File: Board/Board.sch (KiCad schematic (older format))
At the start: 54 parts, among them J1 Screw_Terminal_1x02, P1 USB_B, P2 CONN_01X05, SW1 SW_SPST, SW2 SW_SPST, U1 MCP23016, U2 LM1117-3.3, U3 MCP9808, U4 ESP-12E

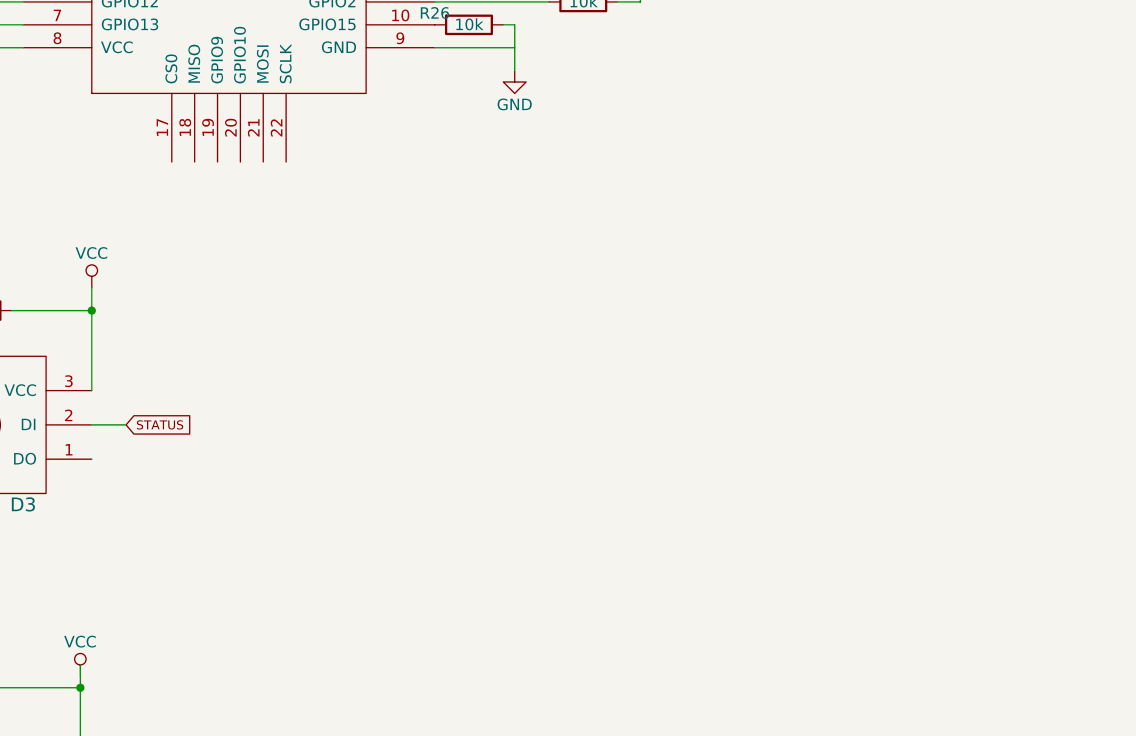
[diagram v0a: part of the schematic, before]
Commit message: Add an SPI connector
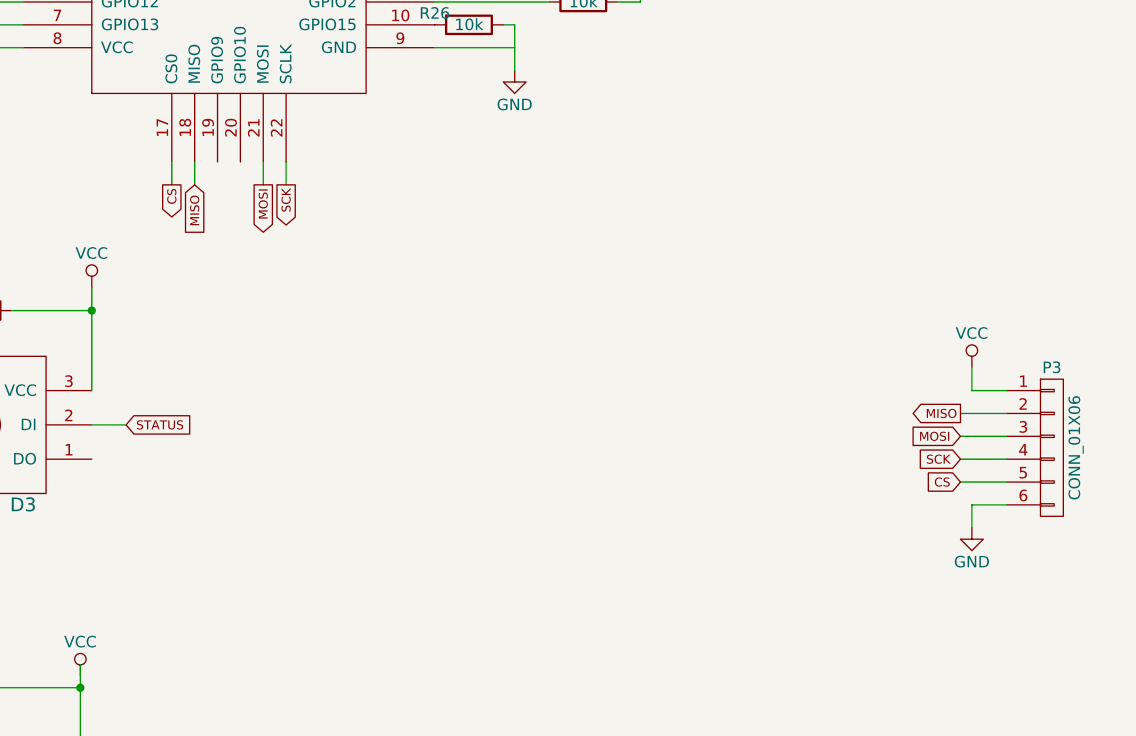
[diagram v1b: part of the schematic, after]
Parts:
- added P3: CONN_01X06, symbol CONN_01X06
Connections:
- net GND: now also P3.6 (P6)
- net VCC: now also P3.1 (P1)
- net CS: now reaches U4.17 (CS0)
- net CS: now also P3.5 (P5)
- net MISO: now reaches U4.18 (MISO)
- net MISO: now also P3.2 (P2)
- net MOSI: now reaches U4.21 (MOSI)
- net MOSI: now also P3.3 (P3)
- net SCK: now reaches U4.22 (SCLK)
- net SCK: now also P3.4 (P4)
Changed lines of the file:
@@
 $EndComp
 $Comp
-L VCC #PWR31
+L VCC #PWR33
 U 1 1 5AD1E910
 P 10400 1300
-F 0 "#PWR31" H 10400 1150 50  0001 C CNN
+F 0 "#PWR33" H 10400 1150 50  0001 C CNN
 F 1 "VCC" H 10400 1450 50  0000 C CNN
 F 2 "" H 10400 1300 50  0000 C CNN
@@
 $EndComp
 $Comp
-L VDD #PWR32
+L VDD #PWR34
 U 1 1 5AD1E925
 P 10600 1300
-F 0 "#PWR32" H 10600 1150 50  0001 C CNN
+F 0 "#PWR34" H 10600 1150 50  0001 C CNN
 F 1 "VDD" H 10600 1450 50  0000 C CNN
 F 2 "" H 10600 1300 50  0000 C CNN
@@
 Wire Wire Line
 	5100 2600 5000 2600
+$Comp
+L GND #PWR32
+U 1 1 5AD82799
+P 10050 5400
+F 0 "#PWR32" H 10050 5150 50  0001 C CNN
+F 1 "GND" H 10050 5250 50  0000 C CNN
+F 2 "" H 10050 5400 50  0000 C CNN
+F 3 "" H 10050 5400 50  0000 C CNN
+	1    10050 5400
+	1    0    0    -1
+$EndComp
+$Comp
+L VCC #PWR31
+U 1 1 5AD8279F
+P 10050 4700
+F 0 "#PWR31" H 10050 4550 50  0001 C CNN
+F 1 "VCC" H 10050 4850 50  0000 C CNN
+F 2 "" H 10050 4700 50  0000 C CNN
+F 3 "" H 10050 4700 50  0000 C CNN
+	1    10050 4700
+	1    0    0    -1
+$EndComp
+Wire Wire Line
+	10050 4700 10050 4800
+Wire Wire Line
+	10050 4800 10200 4800
+Wire Wire Line
+	10050 5400 10050 5300
+Wire Wire Line
+	10050 5300 10200 5300
+Text GLabel 10000 4900 0    39   Output ~ 0
+MISO
+Text GLabel 10000 5000 0    39   Input ~ 0
+MOSI
+Text GLabel 10000 5100 0    39   Input ~ 0
+SCK
+Wire Wire Line
+	10200 4900 10000 4900
+Wire Wire Line
+	10200 5000 10000 5000
+Wire Wire Line
+	10200 5100 10000 5100
+Text GLabel 6650 3900 3    39   Input ~ 0
+MISO
+Wire Wire Line
+	6650 3900 6650 3800
+Text GLabel 6950 3900 3    39   Output ~ 0
+MOSI
+Wire Wire Line
+	6950 3800 6950 3900
+Text GLabel 7050 3900 3    39   Output ~ 0
+SCK
+Wire Wire Line
+	7050 3900 7050 3800
+$Comp
+L CONN_01X06 P3
+U 1 1 5AD852A1
+P 10400 5050
+F 0 "P3" H 10400 5400 50  0000 C CNN
+F 1 "CONN_01X06" V 10500 5050 50  0000 C CNN
+F 2 "" H 10400 5050 50  0000 C CNN
+F 3 "" H 10400 5050 50  0000 C CNN
+	1    10400 5050
+	1    0    0    -1
+$EndComp
+Text GLabel 10000 5200 0    39   Input ~ 0
+CS
+Wire Wire Line
+	10000 5200 10200 5200
+Text GLabel 6550 3900 3    39   Output ~ 0
+CS
+Wire Wire Line
+	6550 3800 6550 3900
 $EndSCHEMATC

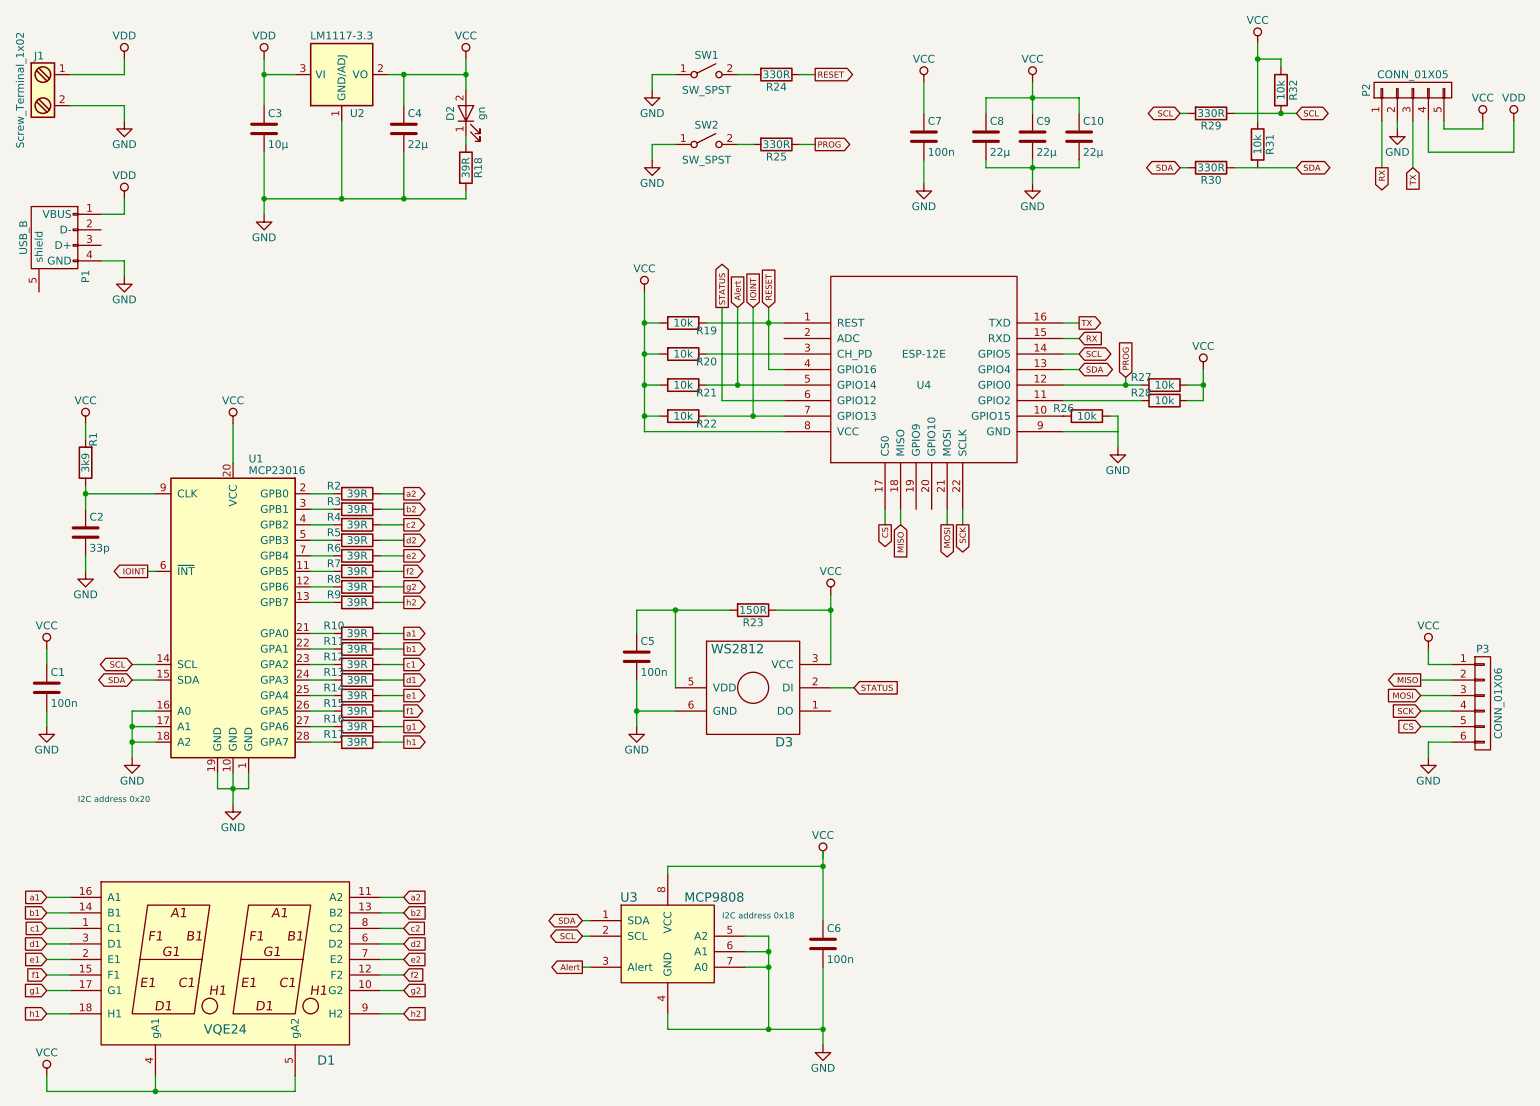
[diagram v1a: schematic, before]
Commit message: Move some things around in the schematic
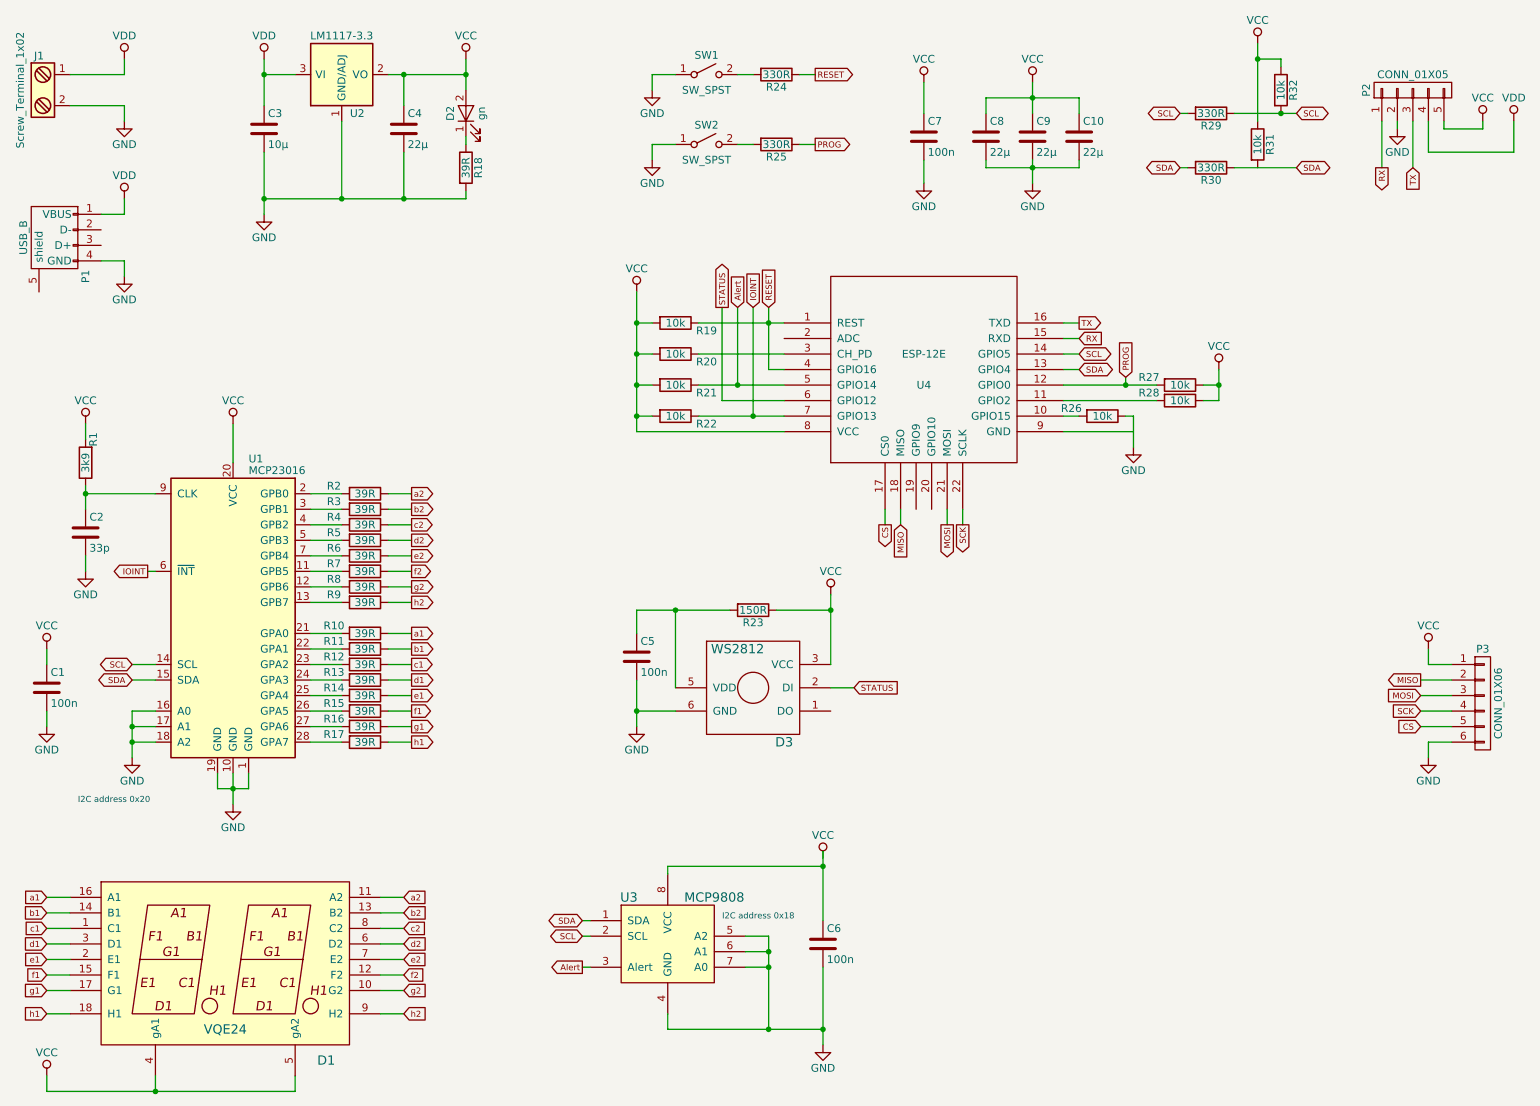
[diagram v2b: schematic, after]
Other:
- moved on the sheet: R10, R11, R12, R13, R14, R15, R16, R17, R19, R2, R20, R21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

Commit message: Remaining footprints
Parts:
- P2: footprint (none) -> Socket_Strips:Socket_Strip_Straight_1x05
- P3: footprint (none) -> Socket_Strips:Socket_Strip_Straight_1x06
- SW1, SW2: footprint (none) -> Buttons_Switches_SMD:SW_SPST_EVQPE1
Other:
- moved on the sheet: R25
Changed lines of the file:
@@
 Sheet 1 1
 Title "Cloud Temperature Sensor"
-Date "2018-04-17"
+Date "2018-04-21"
 Rev ""
 Comp "penguineer"
@@
 $EndComp
 $Comp
-L VCC #PWR17
+L VCC #PWR16
 U 1 1 5AD1E3D6
 P 4950 2400
-F 0 "#PWR17" H 4950 2250 50  0001 C CNN
+F 0 "#PWR16" H 4950 2250 50  0001 C CNN
 F 1 "VCC" H 4950 2550 50  0000 C CNN
 F 2 "" H 4950 2400 50  0000 C CNN
@@
 F 0 "P2" H 9950 1400 50  0000 C CNN
 F 1 "CONN_01X05" V 10050 1100 50  0000 C CNN
-F 2 "" H 9950 1100 50  0000 C CNN
+F 2 "Socket_Strips:Socket_Strip_Straight_1x05" H 9950 1100 50  0001 C CNN
 F 3 "" H 9950 1100 50  0000 C CNN
 	1    9950 1100
@@
 	4950 5100 5200 5100
 $Comp
-L GND #PWR16
+L GND #PWR17
 U 1 1 5AD4FEAF
 P 4950 5200
-F 0 "#PWR16" H 4950 4950 50  0001 C CNN
+F 0 "#PWR17" H 4950 4950 50  0001 C CNN
 F 1 "GND" H 4950 5050 50  0000 C CNN
 F 2 "" H 4950 5200 50  0000 C CNN
@@
 Wire Wire Line
 	3850 1800 3850 1750
-$Comp
-L SW_SPST SW1
-U 1 1 5AD68F78
-P 5400 1000
-F 0 "SW1" H 5400 1125 50  0000 C CNN
-F 1 "SW_SPST" H 5400 900 50  0000 C CNN
-F 2 "" H 5400 1000 50  0000 C CNN
-F 3 "" H 5400 1000 50  0000 C CNN
-	1    5400 1000
-	1    0    0    -1
-$EndComp
 Text GLabel 6100 1000 2    39   Output ~ 0
 RESET
@@
 Wire Wire Line
 	5050 1000 5200 1000
-$Comp
-L SW_SPST SW2
-U 1 1 5AD69C50
-P 5400 1450
-F 0 "SW2" H 5400 1575 50  0000 C CNN
-F 1 "SW_SPST" H 5400 1350 50  0000 C CNN
-F 2 "" H 5400 1450 50  0000 C CNN
-F 3 "" H 5400 1450 50  0000 C CNN
-	1    5400 1450
-	1    0    0    -1
-$EndComp
-Text GLabel 6100 1450 2    39   Output ~ 0
+Text GLabel 6100 1400 2    39   Output ~ 0
 PROG
 Wire Wire Line
-	5600 1450 5700 1450
+	5600 1400 5700 1400
 $Comp
 L GND #PWR19
 U 1 1 5AD69C58
-P 5050 1550
-F 0 "#PWR19" H 5050 1300 50  0001 C CNN
-F 1 "GND" H 5050 1400 50  0000 C CNN
-F 2 "" H 5050 1550 50  0000 C CNN
-F 3 "" H 5050 1550 50  0000 C CNN
-	1    5050 1550
-	1    0    0    -1
-$EndComp
-Wire Wire Line
-	5050 1550 5050 1450
-Wire Wire Line
-	5050 1450 5200 1450
+P 5050 1500
+F 0 "#PWR19" H 5050 1250 50  0001 C CNN
+F 1 "GND" H 5050 1350 50  0000 C CNN
+F 2 "" H 5050 1500 50  0000 C CNN
+F 3 "" H 5050 1500 50  0000 C CNN
+	1    5050 1500
+	1    0    0    -1
+$EndComp
+Wire Wire Line
+	5050 1500 5050 1400
+Wire Wire Line
+	5050 1400 5200 1400
 $Comp
 L R R24
@@
 L R R25
 U 1 1 5AD6C15E
-P 5850 1450
-F 0 "R25" V 5930 1450 50  0000 C CNN
-F 1 "330R" V 5850 1450 50  0000 C CNN
-F 2 "Resistors_SMD:R_0603_HandSoldering" V 5780 1450 50  0001 C CNN
-F 3 "" H 5850 1450 50  0000 C CNN
-	1    5850 1450
+P 5850 1400
+F 0 "R25" V 5930 1400 50  0000 C CNN
+F 1 "330R" V 5850 1400 50  0000 C CNN
+F 2 "Resistors_SMD:R_0603_HandSoldering" V 5780 1400 50  0001 C CNN
+F 3 "" H 5850 1400 50  0000 C CNN
+	1    5850 1400
 	0    1    1    0
 $EndComp
@@
 	6000 1000 6100 1000
 Wire Wire Line
-	6000 1450 6100 1450
+	6000 1400 6100 1400
 Wire Wire Line
 	5700 2500 5700 3200
@@
 F 0 "P3" H 10400 5400 50  0000 C CNN
 F 1 "CONN_01X06" V 10500 5050 50  0000 C CNN
-F 2 "" H 10400 5050 50  0000 C CNN
+F 2 "Socket_Strips:Socket_Strip_Straight_1x06" H 10400 5050 50  0001 C CNN
 F 3 "" H 10400 5050 50  0000 C CNN
 	1    10400 5050
@@
 Wire Wire Line
 	7800 3200 7700 3200
+$Comp
+L SW_SPST SW1
+U 1 1 5AD68F78
+P 5400 1000
+F 0 "SW1" H 5400 1125 50  0000 C CNN
+F 1 "SW_SPST" H 5400 900 50  0000 C CNN
+F 2 "Buttons_Switches_SMD:SW_SPST_EVQPE1" H 5400 1000 50  0001 C CNN
+F 3 "" H 5400 1000 50  0000 C CNN
+	1    5400 1000
+	1    0    0    -1
+$EndComp
+$Comp
+L SW_SPST SW2
+U 1 1 5ADB847E
+P 5400 1400
+F 0 "SW2" H 5400 1525 50  0000 C CNN
+F 1 "SW_SPST" H 5400 1300 50  0000 C CNN
+F 2 "Buttons_Switches_SMD:SW_SPST_EVQPE1" H 5400 1400 50  0001 C CNN
+F 3 "" H 5400 1400 50  0000 C CNN
+	1    5400 1400
+	1    0    0    -1
+$EndComp
 $EndSCHEMATC
